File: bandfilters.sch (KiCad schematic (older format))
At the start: 26 parts

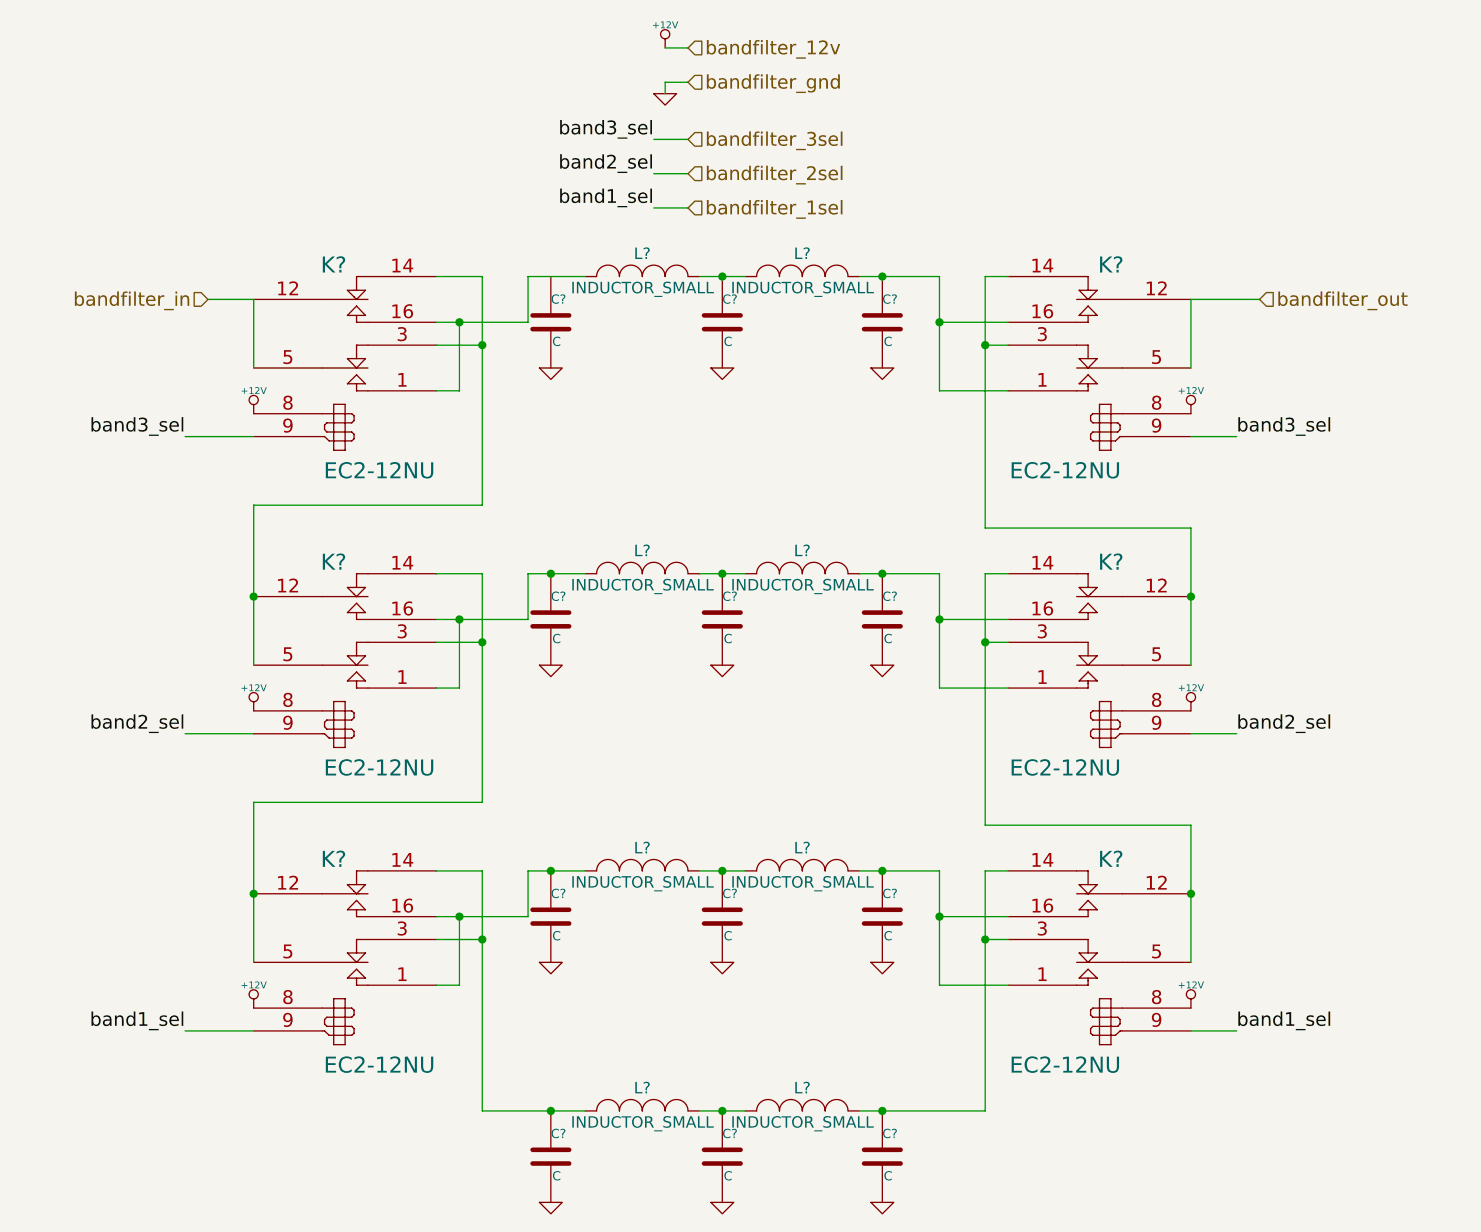
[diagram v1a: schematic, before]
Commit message: Annotated all schematics
- Added more caps to power supply
- Decided on power supply fuse part
- Changed 1n5711 SWR caps to BAT62
- Decided on MMBF170 for amp bias switch
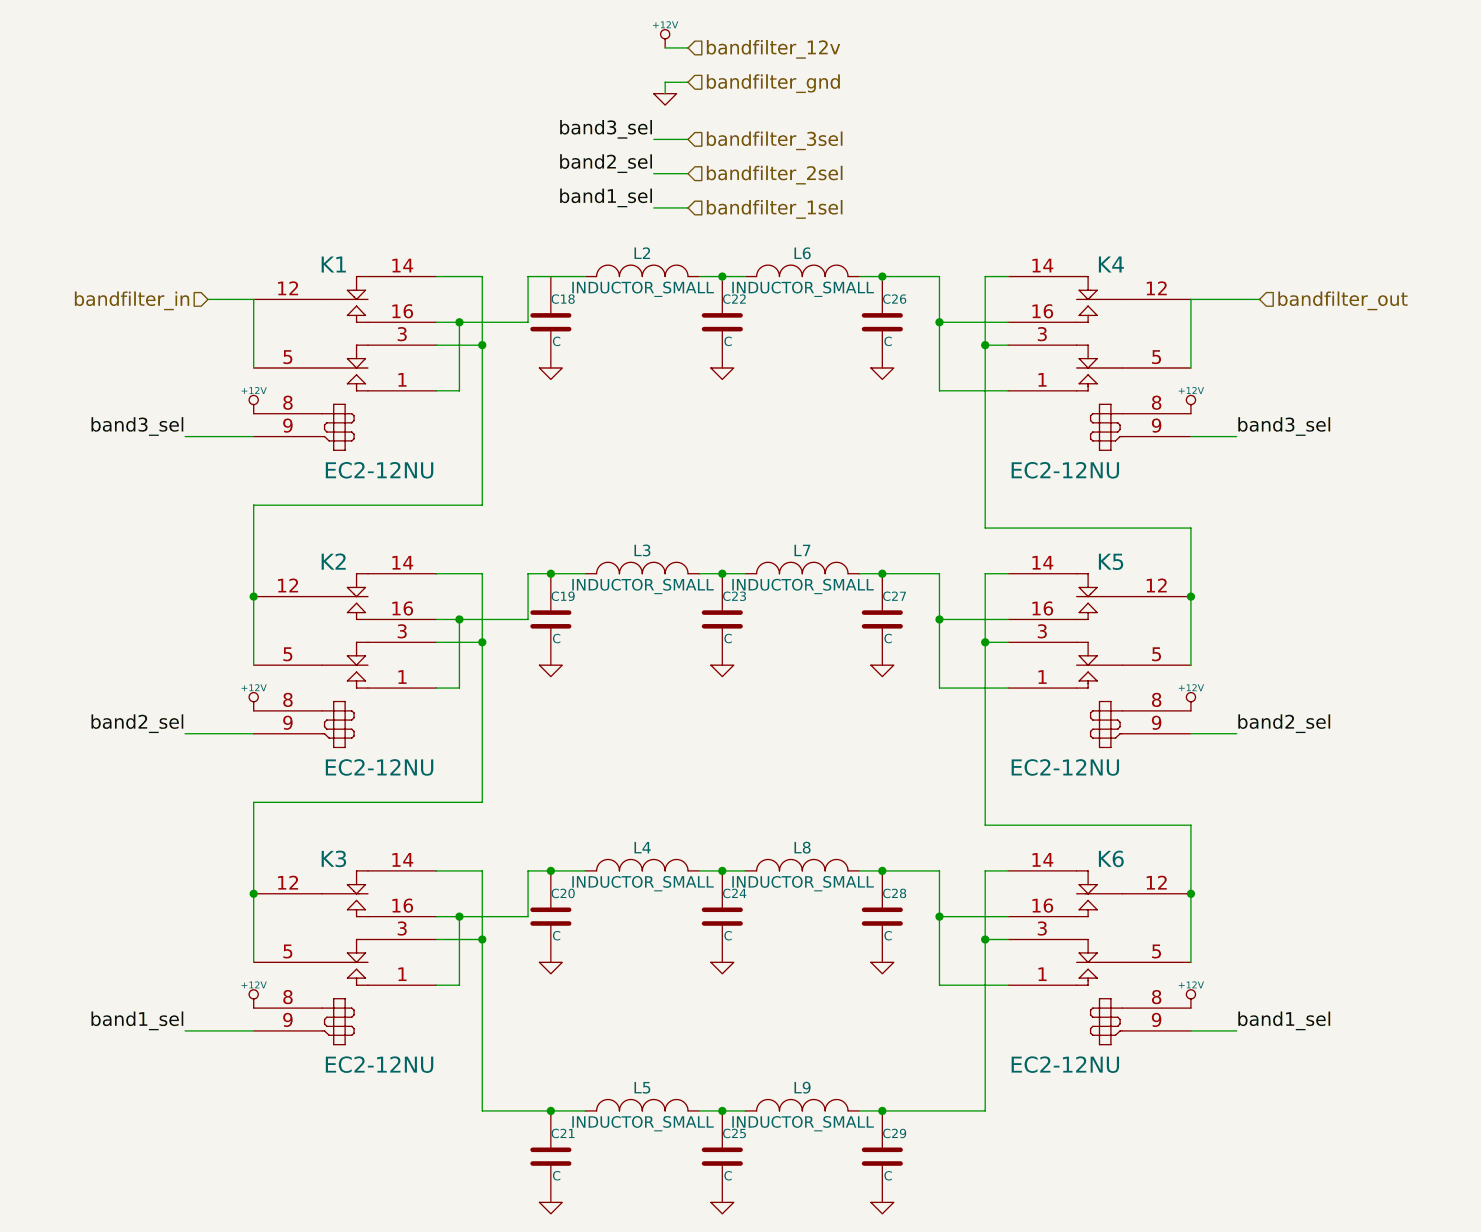
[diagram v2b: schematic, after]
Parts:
- gave numbers to parts that had none: 26

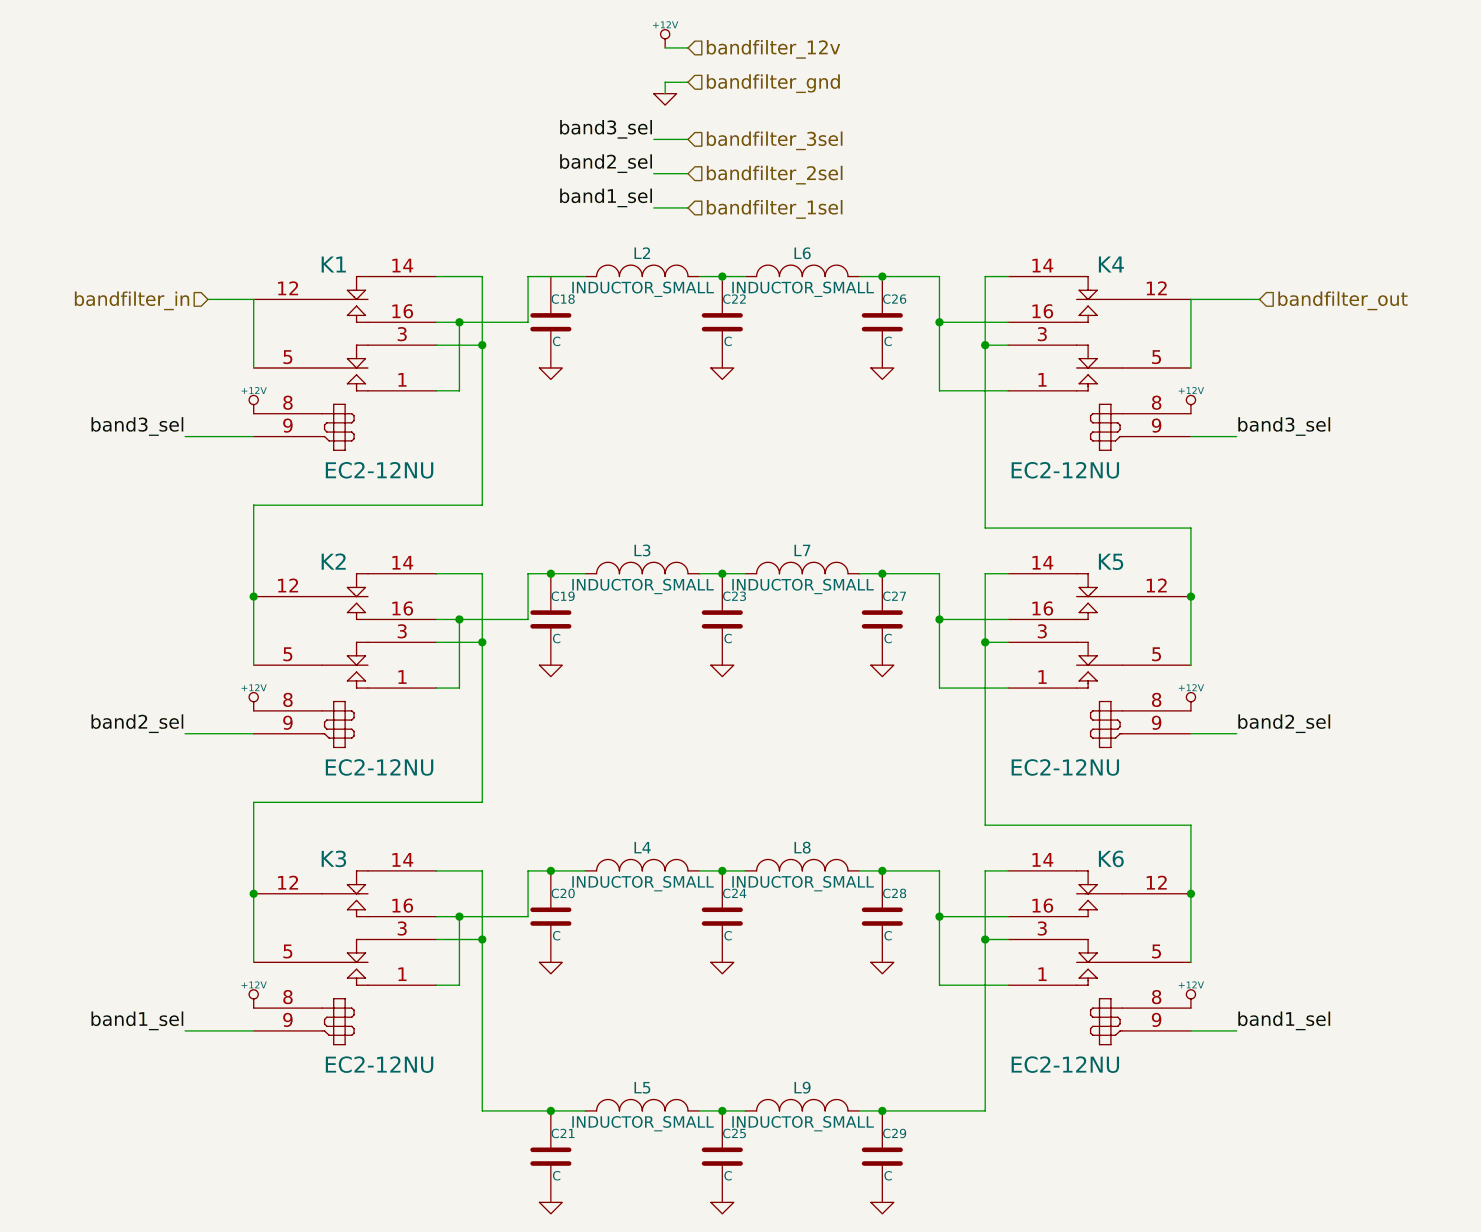
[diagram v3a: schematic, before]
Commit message: Finished band filters schematic
- Associated last of the capacitors with footprints
- Associated inductors
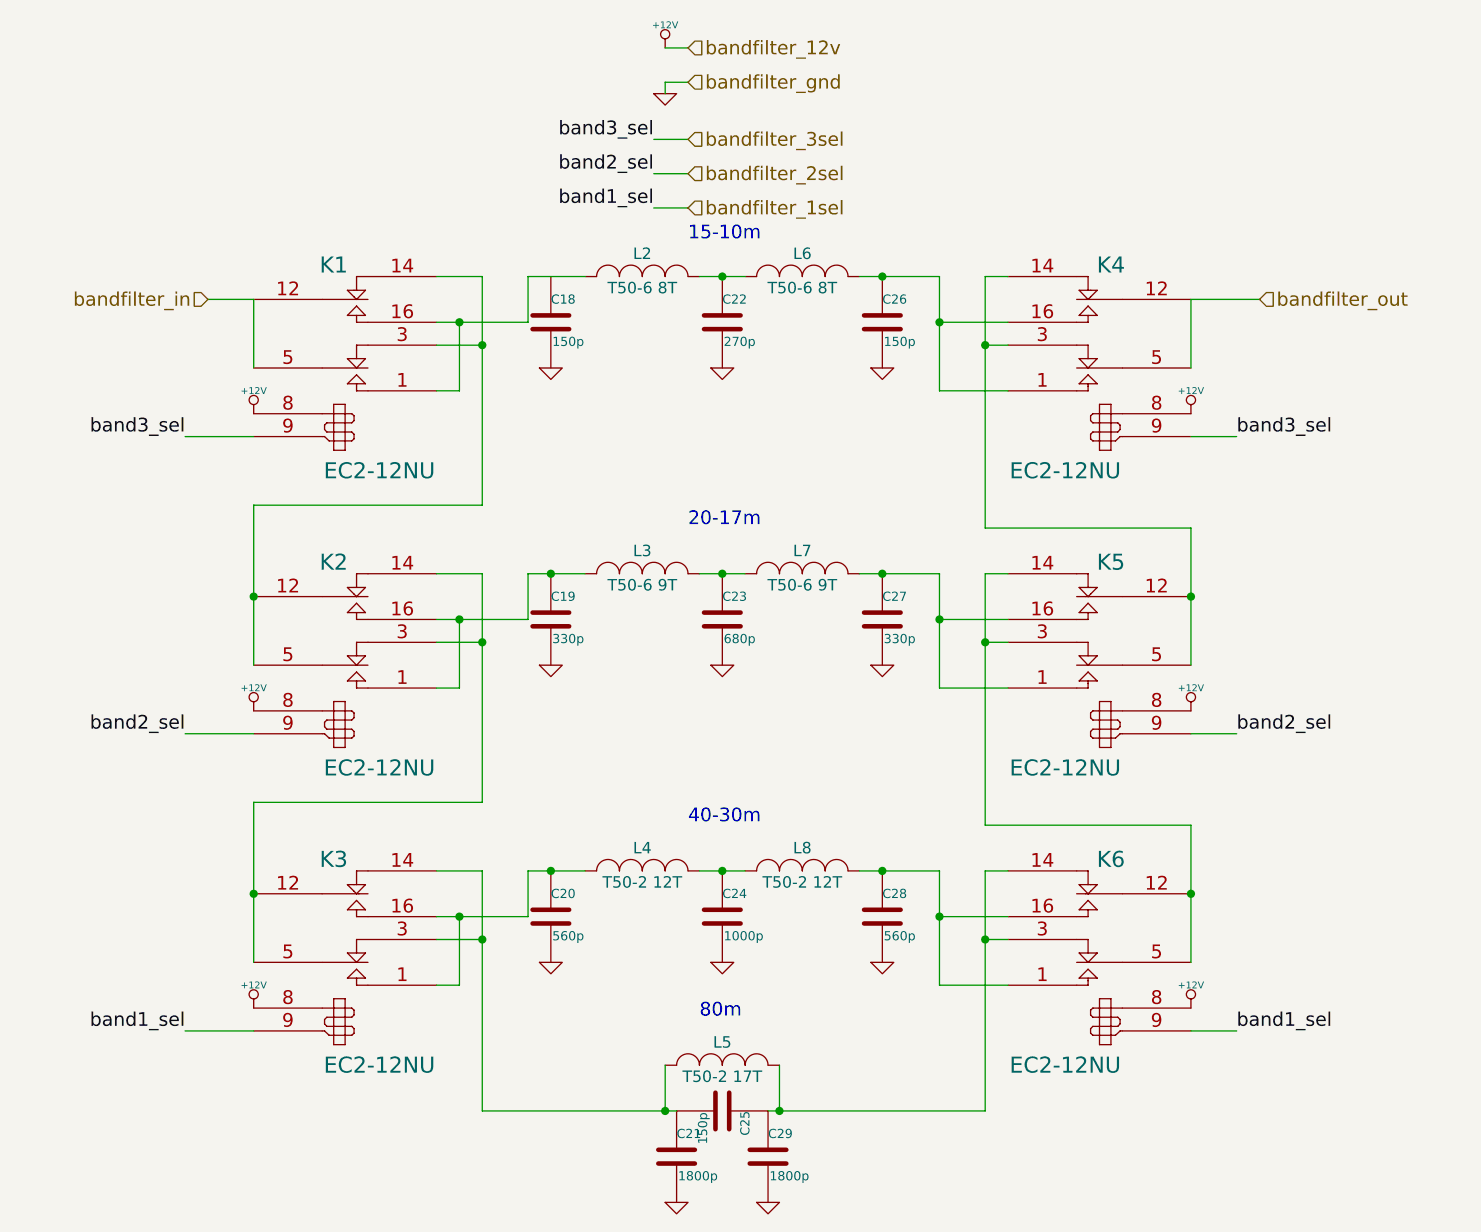
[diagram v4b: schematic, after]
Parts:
- removed L9: INDUCTOR_SMALL, symbol INDUCTOR_SMALL
- C18, C25, C26: value C -> 150p
- C19, C27: value C -> 330p
- C20, C28: value C -> 560p
- C21, C29: value C -> 1800p
- C22: value C -> 270p
- C23: value C -> 680p
- C24: value C -> 1000p
- L2, L6: value INDUCTOR_SMALL -> T50-6 8T
- L3, L7: value INDUCTOR_SMALL -> T50-6 9T
- L4, L8: value INDUCTOR_SMALL -> T50-2 12T
- L5: value INDUCTOR_SMALL -> T50-2 17T
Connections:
- net GND: no longer C25.2
- net at C21.1, K3.14 (R2), K3.3 (R1)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: now also C25.2
- net at C25.1, L5.2: now also C29.1, K6.14 (R2), K6.3 (R1)
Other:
- note added: "15-10m"
- note added: "20-17m"
- note added: "40-30m"
- note added: "80m"
- moved on the sheet: C21, C25, C29, L5

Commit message: Finished associating relays
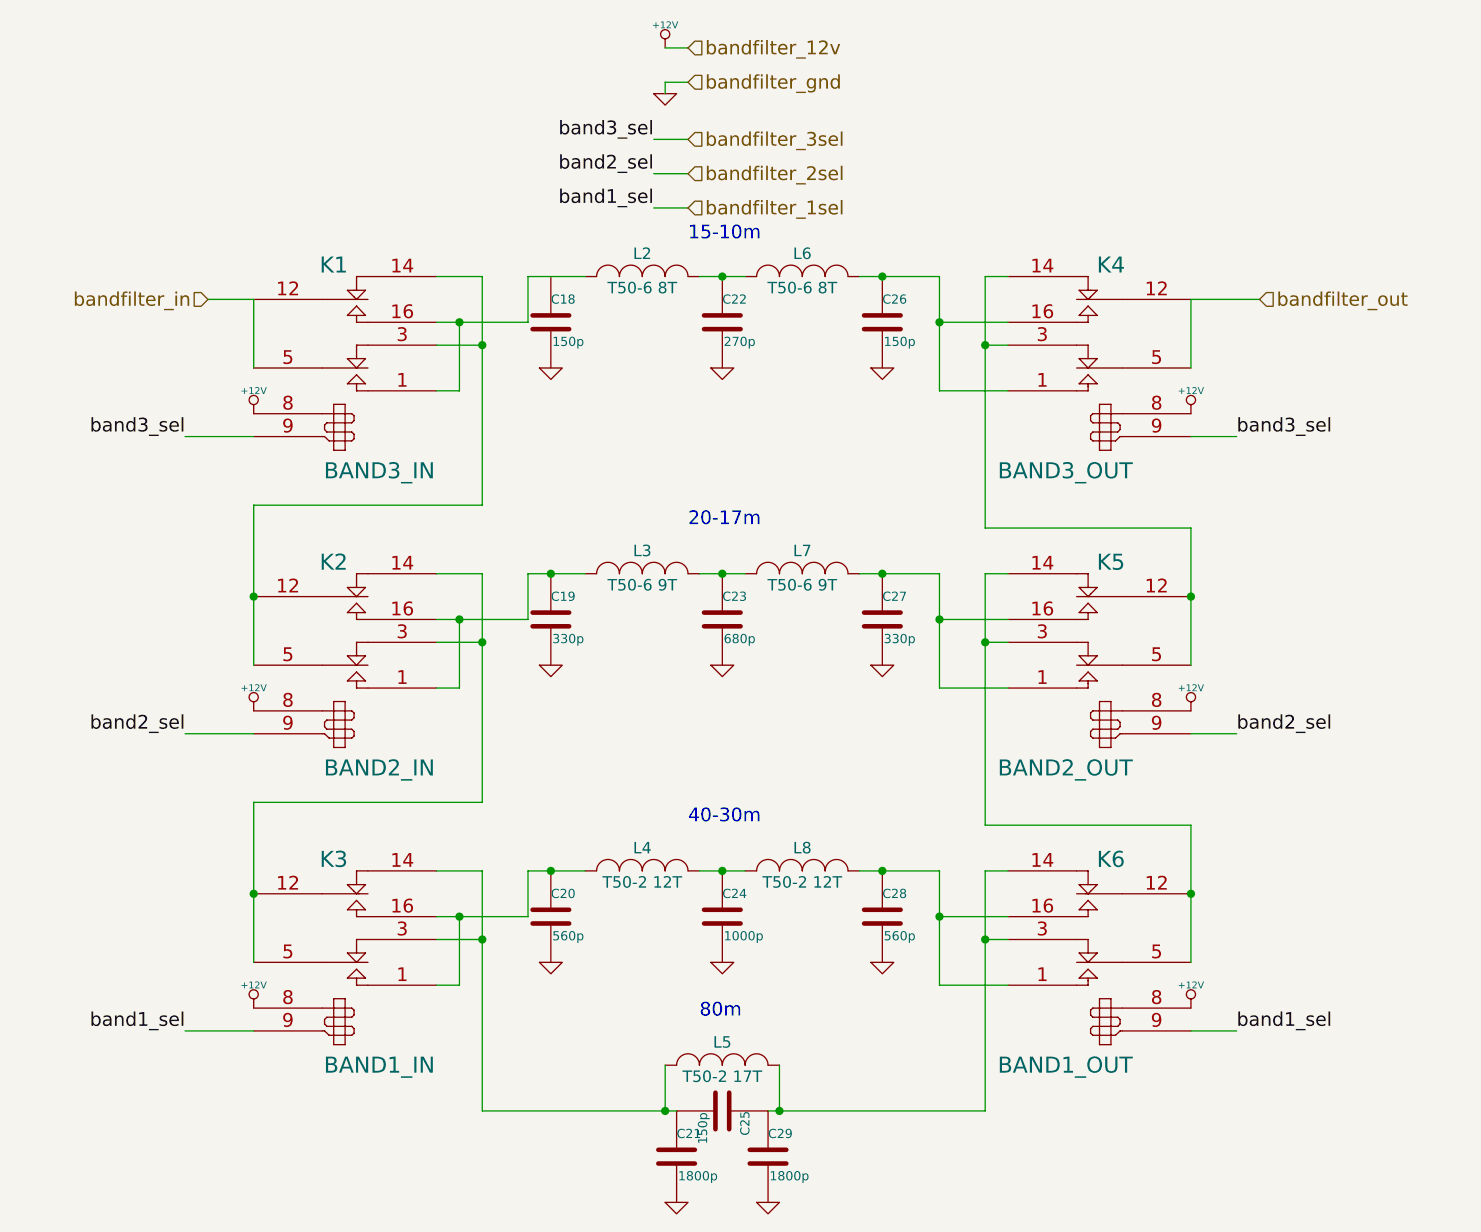
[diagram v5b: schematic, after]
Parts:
- C18, C19, C20, C21, C22, C23, C24, C25, C26, C27, C28, C29: footprint (none) -> Discret:C1
- K1: value EC2-12NU -> BAND3_IN; footprint (none) -> nu9j-footprints:EC2-12NU
- K2: value EC2-12NU -> BAND2_IN; footprint (none) -> nu9j-footprints:EC2-12NU
- K3: value EC2-12NU -> BAND1_IN; footprint (none) -> nu9j-footprints:EC2-12NU
- K4: value EC2-12NU -> BAND3_OUT; footprint (none) -> nu9j-footprints:EC2-12NU
- K5: value EC2-12NU -> BAND2_OUT; footprint (none) -> nu9j-footprints:EC2-12NU
- K6: value EC2-12NU -> BAND1_OUT; footprint (none) -> nu9j-footprints:EC2-12NU
- L2, L3, L4, L5, L6, L7, L8: footprint (none) -> nu9j-footprints:TOROID-50
